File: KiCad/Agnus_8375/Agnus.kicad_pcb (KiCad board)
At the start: 4 copper layers, 29.3 x 29.3 mm, 28 parts, among them J6 Conn_01x01, U1 10M02SCU169C8G, U2 LM1117-3.3, U3 SN74CBTD16210, U4 SN74CBTD16210, U5 SN74CBTD16210, U6 SN74CBTD16210, U7 Agnus_8375_MB_socket

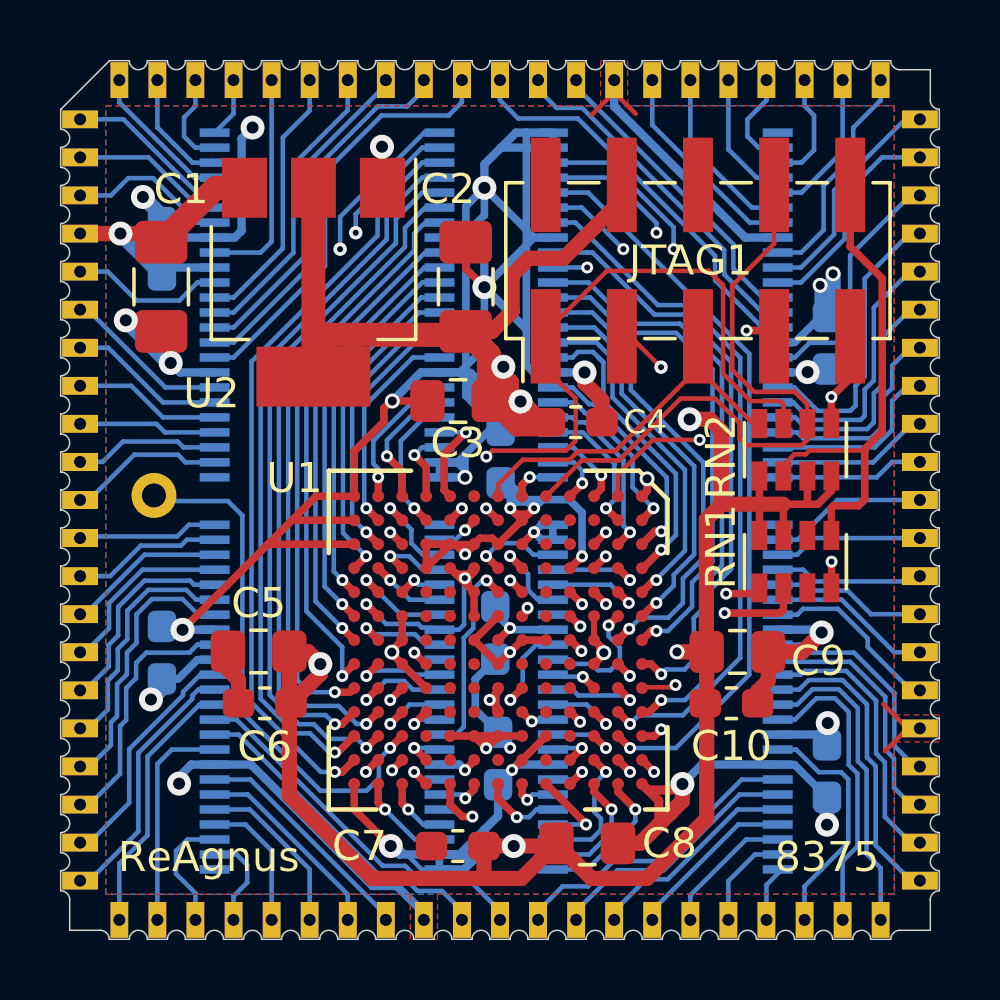
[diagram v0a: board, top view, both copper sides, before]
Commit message: Made custom footprint with smaller pads 1.0mm -> 0.8mm, allowing for more centered TDO and CASL vias
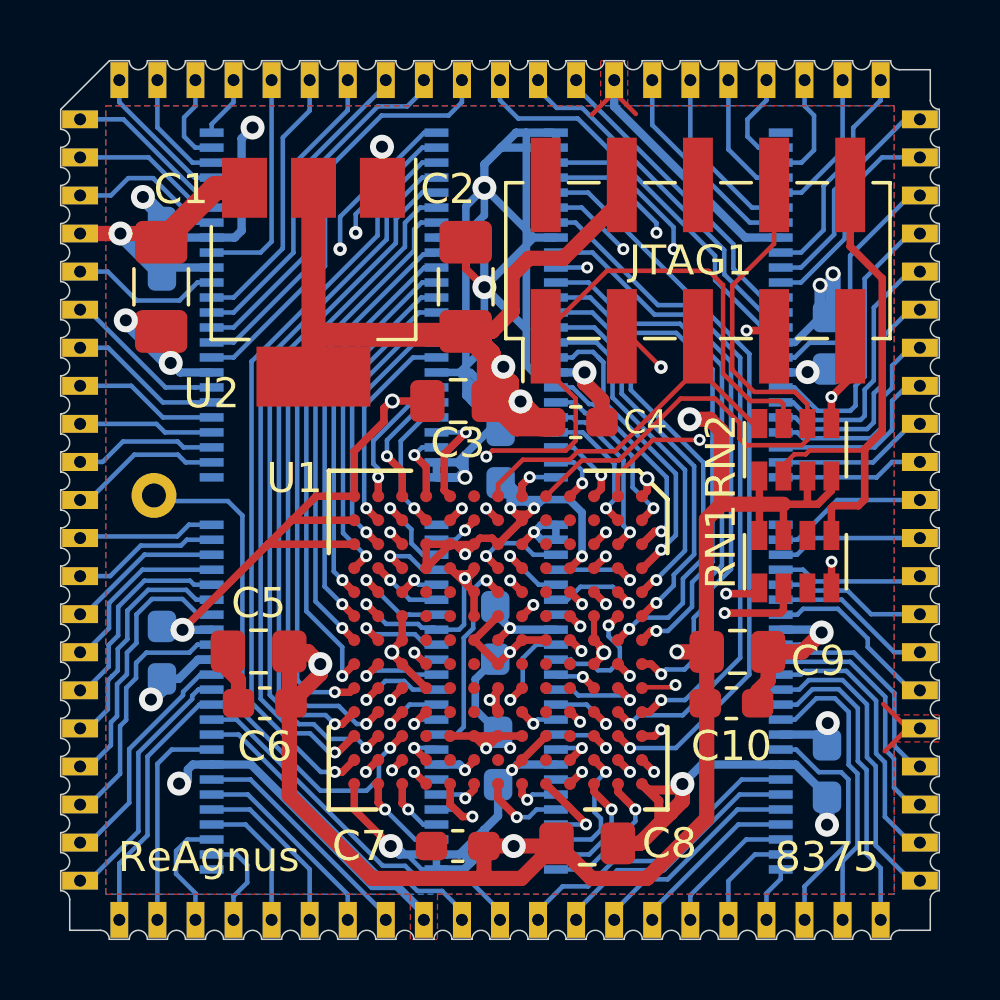
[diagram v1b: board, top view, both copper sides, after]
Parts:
- U3, U4, U5, U6: footprint Package_SO:TSSOP-48_6.1x12.5mm_P0.5mm -> Agnus:TSSOP-48_6.1x12.5mm_P0.5mm_padLength_0.8mm
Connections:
- U1 pad B5: A3_FPGA -> A2_FPGA
- U1 pad F4: A2_FPGA -> A3_FPGA
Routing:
- net GND: track 224.7 -> 223.0 mm
- net A3_FPGA: track 3.29 -> 2.50 mm

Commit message: Added more decoupling caps, changed to 6 mil copper pour clearance, added some more 3V3/GND vias, improved routing.
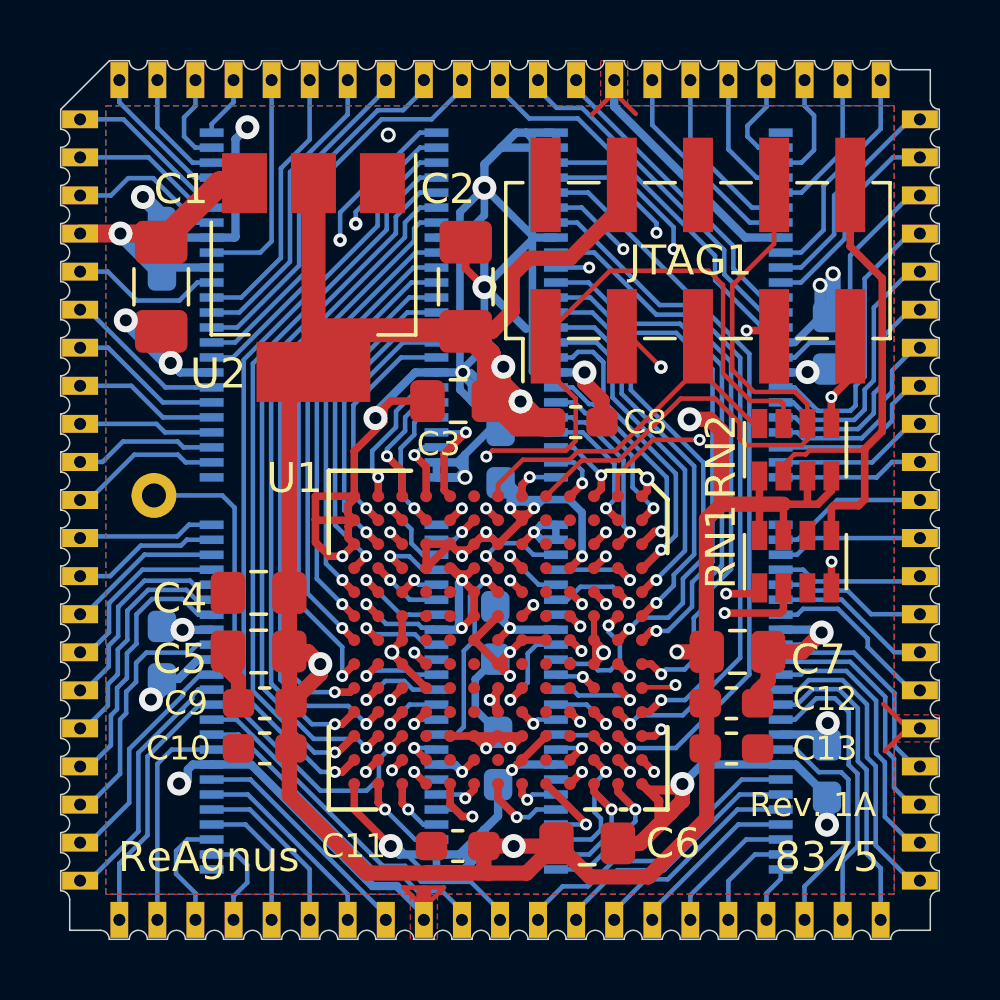
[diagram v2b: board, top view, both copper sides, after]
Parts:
- removed the C9 at (152.6, 79.7)
- added C10: 0.01uF, Capacitor_SMD:C_0603_1608Metric_Pad1.05x0.95mm_HandSolder, F.Cu at (136.8, 82.9)
- added C13: 0.01uF, Capacitor_SMD:C_0603_1608Metric_Pad1.05x0.95mm_HandSolder, F.Cu at (152.4, 82.9)
- added C6: 0.1uF, Capacitor_SMD:C_0805_2012Metric_Pad1.15x1.40mm_HandSolder, F.Cu at (147.6, 86.1)
- added C7: 0.1uF, Capacitor_SMD:C_0805_2012Metric_Pad1.15x1.40mm_HandSolder, F.Cu at (152.6, 79.7)
- moved C5 12.7 mm to (136.6, 79.7), turned to 0 degrees
- moved C4 1.96 mm to (136.6, 77.8)
- moved U2 0.16 mm to (138.4, 67.2)
- renumbered C7 to C11, C10 to C12, C11 to C14, C12 to C15, C13 to C16, C14 to C17, C15 to C18, C16 to C19, C17 to C20, C5 to C4, C8 to C5, C4 to C8, C6 to C9
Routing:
- net 3V3: track 212.8 -> 153.8 mm, vias 16 -> 18
- net GND: track 223.0 -> 204.1 mm, vias 30 -> 33
- net INTR_FPGA: track 7.08 -> 7.71 mm
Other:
- board text added: "Rev. 1A"
